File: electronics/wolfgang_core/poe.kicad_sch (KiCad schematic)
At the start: 0 parts

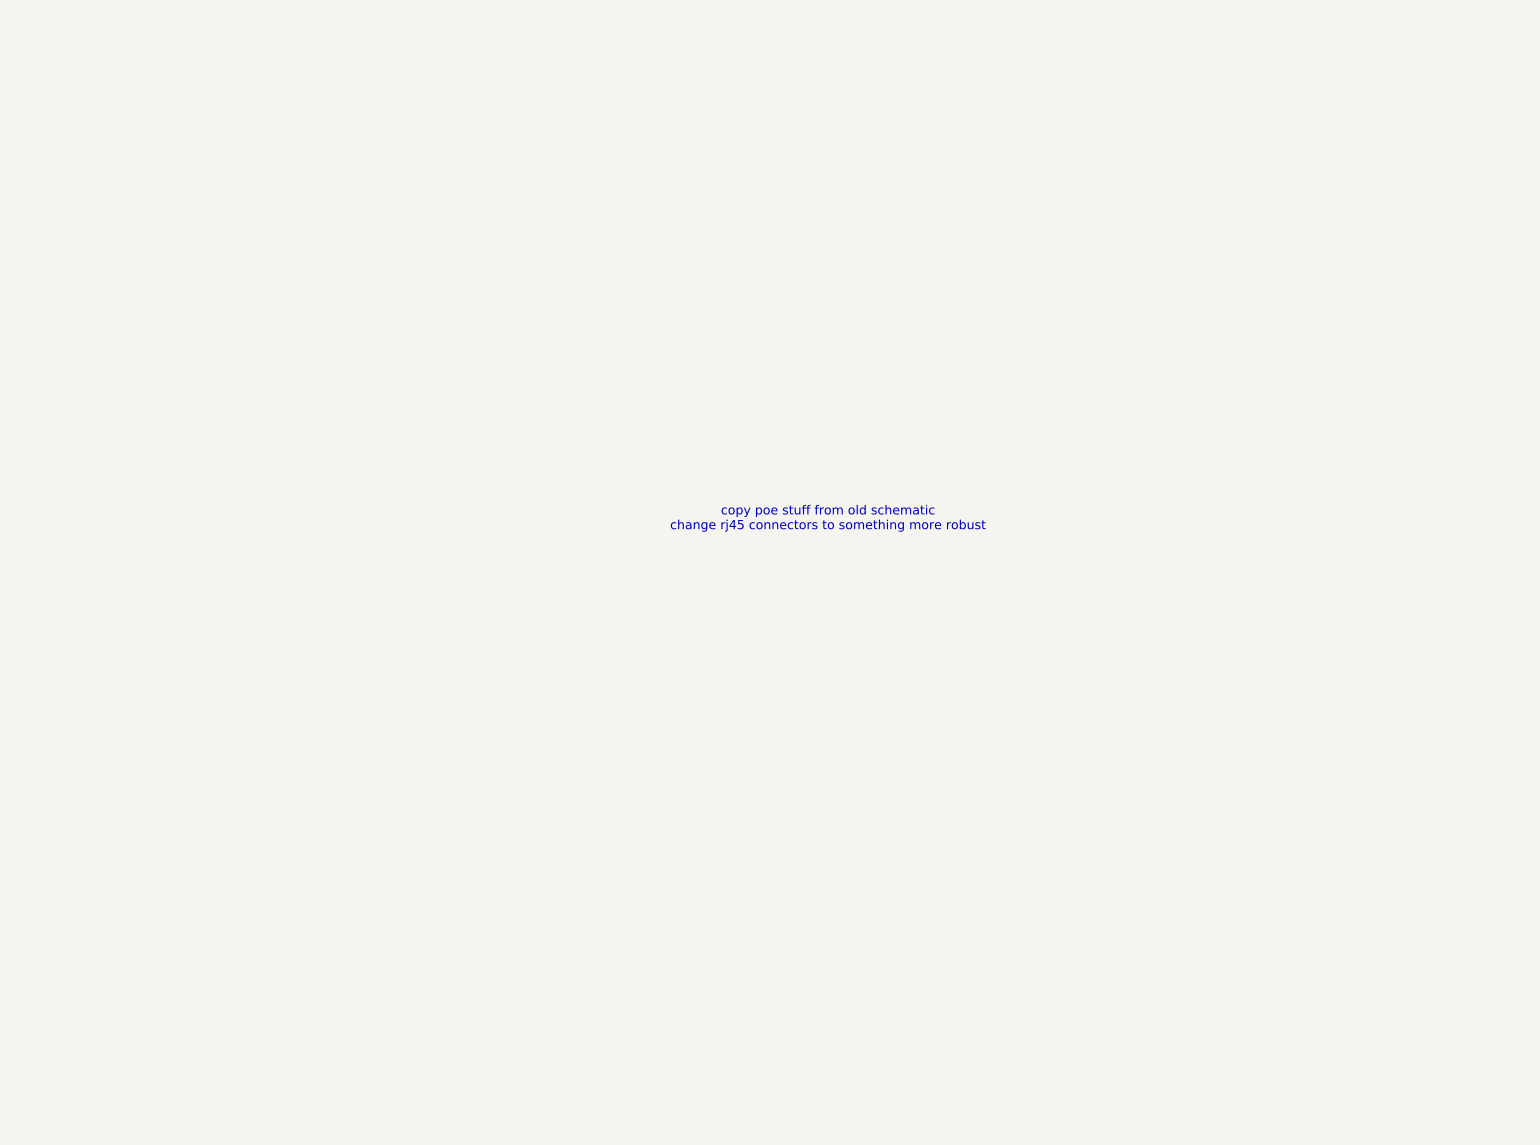
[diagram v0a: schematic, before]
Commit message: Copy over PoE stuff
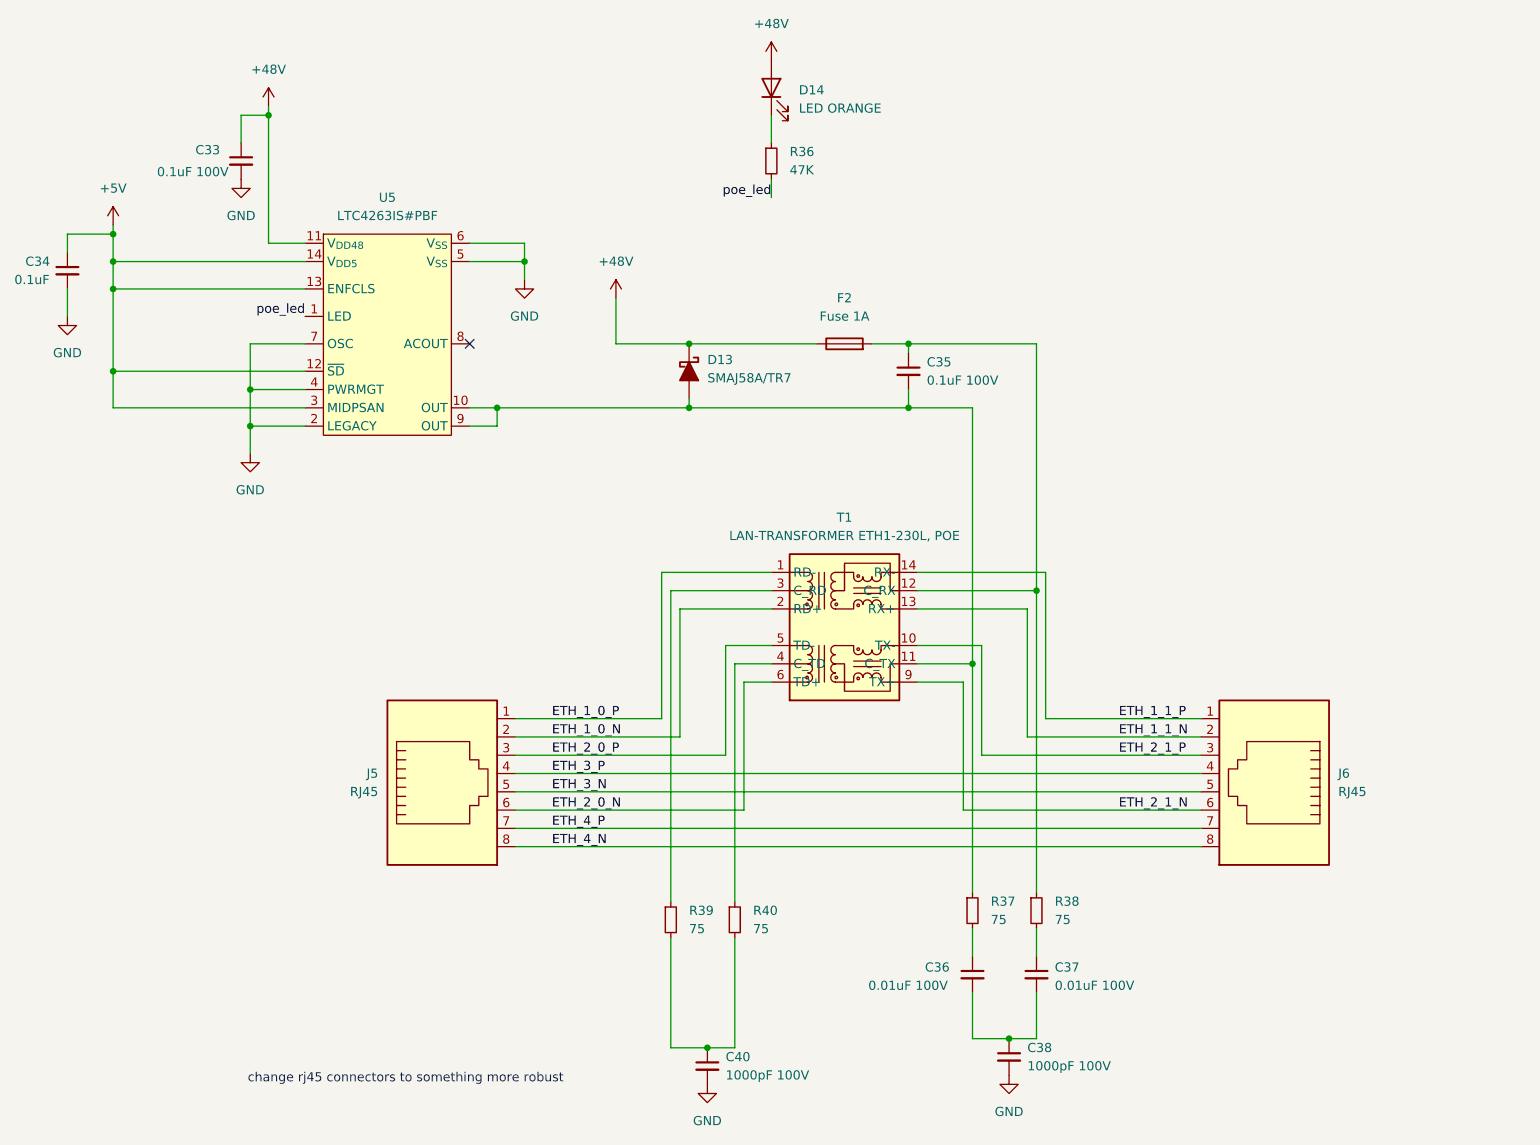
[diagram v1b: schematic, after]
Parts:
- added C33, C35: 0.1uF 100V, symbol Device:C_Small
- added C34: 0.1uF, symbol Device:C_Small
- added C36, C37: 0.01uF 100V, symbol Device:C_Small
- added C38, C40: 1000pF 100V, symbol Device:C_Small
- added D13: SMAJ58A/TR7, symbol Device:D_Schottky_Filled
- added D14: LED ORANGE, symbol Device:LED
- added F2: Fuse 1A, symbol Device:Fuse
- added J5, J6: RJ45, symbol Connector:RJ45
- added R36: 47K, symbol Device:R_Small
- added R37, R38, R39, R40: 75, symbol Device:R_Small
- added T1: LAN-TRANSFORMER ETH1-230L, POE, symbol ETH1-230LD-POE:ETH1-230LD-POE
- added U5: LTC4263IS#PBF, symbol ltc4263:ltc4263
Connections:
- new net: D14.1 (K), R36.1
- new net: C36.2, C37.2, C38.1
- new net: R40.1, T1.4 (C_TD)
- new net: C40.1, R39.2, R40.2
- new net: C35.2, D13.2 (A), R37.1, T1.11 (C_TX), U5.10 (OUT), U5.9 (OUT)
- new net: C36.1, R37.2
- new net: C35.1, F2.2, R38.1, T1.12 (C_RX)
- new net: C37.1, R38.2
- new net: R39.1, T1.3 (C_RD)
- new net +48V: C33.1, D13.1 (K), D14.2 (A), F2.1, U5.11 (V_{DD48})
- new net +5V: C34.1, U5.12 (~{SD}), U5.13 (ENFCLS), U5.14 (V_{DD5}), U5.3 (MIDPSAN)
- new net ETH_1_0_N: J5.2, T1.2 (RD+)
- new net ETH_1_0_P: J5.1, T1.1 (RD-)
- new net ETH_1_1_N: J6.2, T1.13 (RX+)
- new net ETH_1_1_P: J6.1, T1.14 (RX-)
- new net ETH_2_0_N: J5.6, T1.6 (TD+)
- new net ETH_2_0_P: J5.3, T1.5 (TD-)
- new net ETH_2_1_N: J6.6, T1.9 (TX+)
- new net ETH_2_1_P: J6.3, T1.10 (TX-)
- new net ETH_3_N: J5.5, J6.5
- new net ETH_3_P: J5.4, J6.4
- new net ETH_4_N: J5.8, J6.8
- new net ETH_4_P: J5.7, J6.7
- new net GND: C33.2, C34.2, C38.2, C40.2, U5.2 (LEGACY), U5.4 (PWRMGT), U5.5 (V_{SS}), U5.6 (V_{SS}), U5.7 (OSC)
- new net Pad: U5.15 (Pad)
- new net poe_led: R36.2, U5.1 (LED)
- no-connect marks 0 -> 1
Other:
- note added: "change rj45 connectors to something more robust"
- note removed: "copy poe stuff from old schematic change rj45 connectors to something more robust"

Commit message: Footprints hinzugefügt
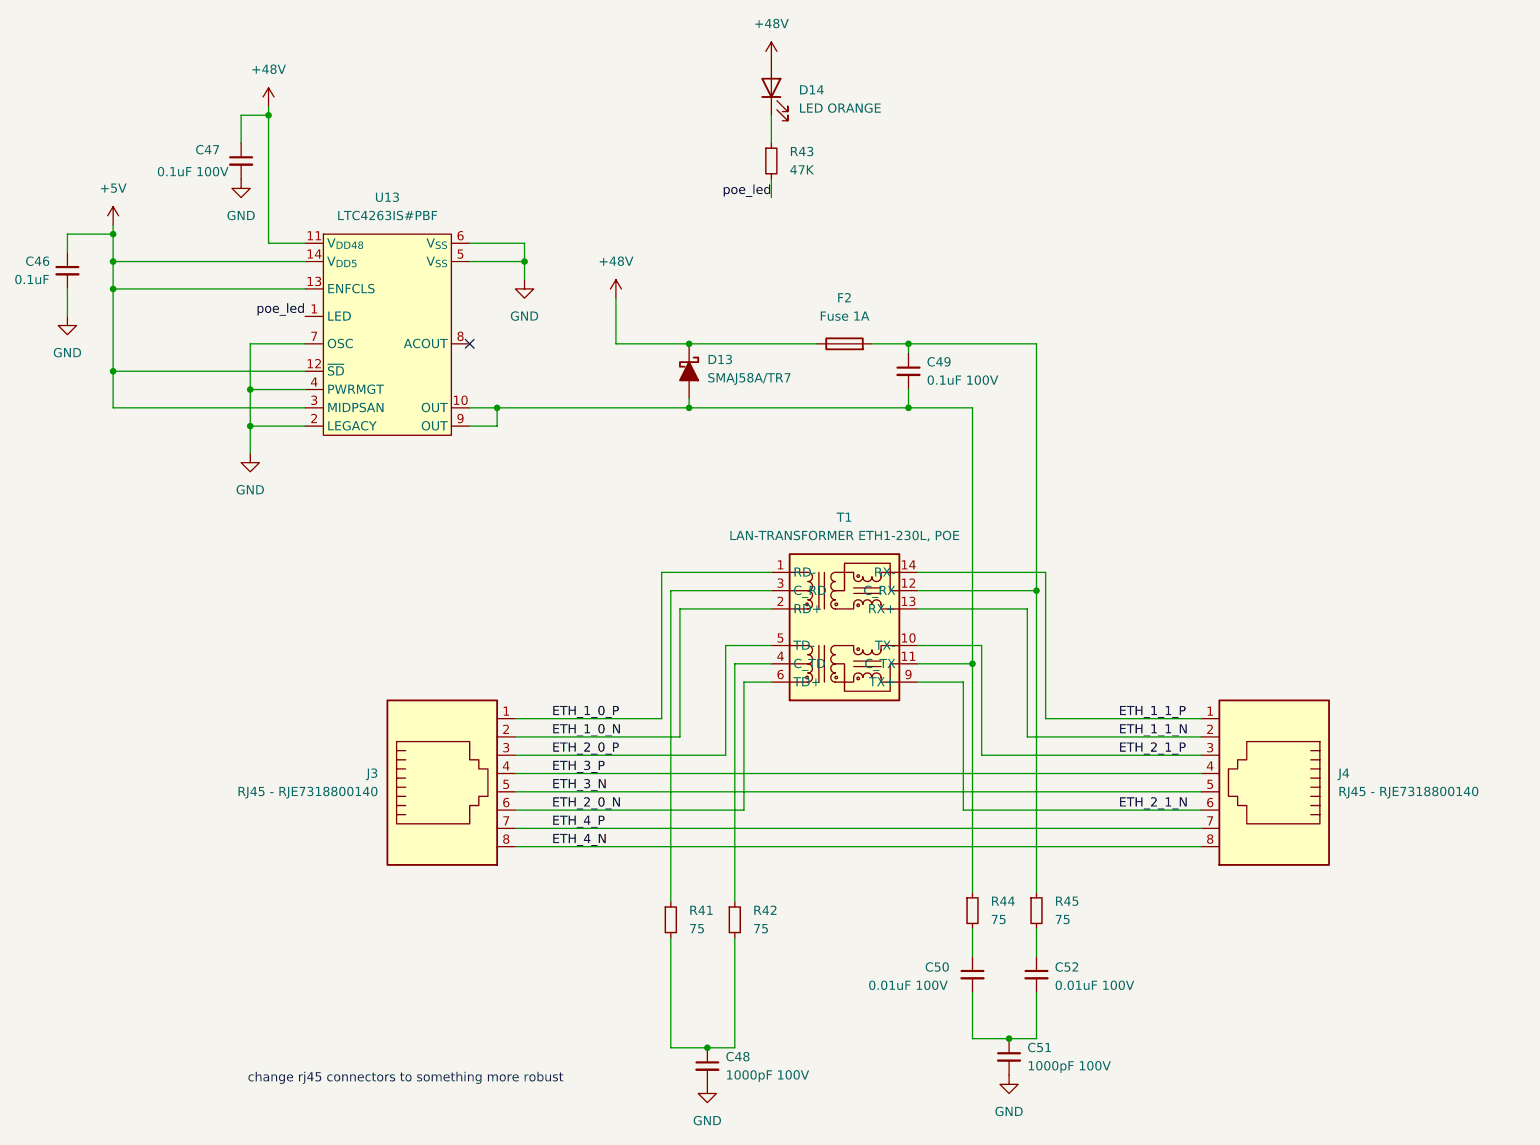
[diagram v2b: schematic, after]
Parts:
- J3: renamed from J5; value RJ45 -> RJ45 - RJE7318800140; footprint (none) -> bitbots:RJE7318800110
- J4: renamed from J6; value RJ45 -> RJ45 - RJE7318800140; footprint (none) -> bitbots:RJE7318800110
- T1: footprint (none) -> bitbots:ETH1230LD
- U13: renamed from U5; footprint (none) -> bitbots:SOIC127P599X175-14N
- renumbered C34 to C46, C33 to C47, C40 to C48, C35 to C49, C36 to C50, C38 to C51, C37 to C52, R39 to R41, R40 to R42, R36 to R43, R37 to R44, R38 to R45
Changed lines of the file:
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@@
 		(dnp no)
 		(fields_autoplaced yes)
-		(property "Reference" "R36"
+		(property "Reference" "R43"
 			(at 123.19 34.2899 0)
 			(effects
@@
 			(project ""
 				(path "/9538e4ed-27e6-4c37-b989-9859dc0d49e8/3d827942-3ef6-4515-bd08-bedcdbccf816"
-					(reference "R36")
+					(reference "R43")
 					(unit 1)
 				)
@@
 		(dnp no)
 		(fields_autoplaced yes)
-		(property "Reference" "C38"
+		(property "Reference" "C51"
 			(at 156.21 158.7562 0)
 			(effects
@@
 			(project ""
 				(path "/9538e4ed-27e6-4c37-b989-9859dc0d49e8/3d827942-3ef6-4515-bd08-bedcdbccf816"
-					(reference "C38")
+					(reference "C51")
 					(unit 1)
 				)
@@
 		(dnp no)
 		(fields_autoplaced yes)
-		(property "Reference" "R40"
+		(property "Reference" "R42"
 			(at 118.11 139.6999 0)
 			(effects
@@
 			(project "wolfgang_core"
 				(path "/9538e4ed-27e6-4c37-b989-9859dc0d49e8/3d827942-3ef6-4515-bd08-bedcdbccf816"
-					(reference "R40")
+					(reference "R42")
 					(unit 1)
 				)
@@
 		(dnp no)
 		(fields_autoplaced yes)
-		(property "Reference" "#PWR090"
+		(property "Reference" "#PWR0108"
 			(at 111.76 170.18 0)
 			(effects
@@
 			(project "wolfgang_core"
 				(path "/9538e4ed-27e6-4c37-b989-9859dc0d49e8/3d827942-3ef6-4515-bd08-bedcdbccf816"
-					(reference "#PWR090")
+					(reference "#PWR0108")
 					(unit 1)
 				)
@@
 		(dnp no)
 		(fields_autoplaced yes)
-		(property "Reference" "U5"
+		(property "Reference" "U13"
 			(at 67.31 40.64 0)
 			(effects
@@
 			)
 		)
-		(property "Footprint" ""
+		(property "Footprint" "bitbots:SOIC127P599X175-14N"
 			(at 66.04 55.88 0)
 			(effects
@@
 			(project ""
 				(path "/9538e4ed-27e6-4c37-b989-9859dc0d49e8/3d827942-3ef6-4515-bd08-bedcdbccf816"
-					(reference "U5")
+					(reference "U13")
 					(unit 1)
 				)
@@
 		(dnp no)
 		(fields_autoplaced yes)
-		(property "Reference" "R37"
+		(property "Reference" "R44"
 			(at 151.13 138.4299 0)
 			(effects
@@
 			(project ""
 				(path "/9538e4ed-27e6-4c37-b989-9859dc0d49e8/3d827942-3ef6-4515-bd08-bedcdbccf816"
-					(reference "R37")
+					(reference "R44")
 					(unit 1)
 				)
@@
 		(dnp no)
 		(fields_autoplaced yes)
-		(property "Reference" "#PWR083"
+		(property "Reference" "#PWR0102"
 			(at 29.21 48.26 0)
 			(effects
@@
 			(project ""
 				(path "/9538e4ed-27e6-4c37-b989-9859dc0d49e8/3d827942-3ef6-4515-bd08-bedcdbccf816"
-					(reference "#PWR083")
+					(reference "#PWR0102")
 					(unit 1)
 				)
@@
 		(dnp no)
 		(fields_autoplaced yes)
-		(property "Reference" "#PWR085"
+		(property "Reference" "#PWR0106"
 			(at 86.36 58.42 0)
 			(effects
@@
 			(project ""
 				(path "/9538e4ed-27e6-4c37-b989-9859dc0d49e8/3d827942-3ef6-4515-bd08-bedcdbccf816"
-					(reference "#PWR085")
+					(reference "#PWR0106")
 					(unit 1)
 				)
@@
 		(dnp no)
 		(fields_autoplaced yes)
-		(property "Reference" "#PWR086"
+		(property "Reference" "#PWR0107"
 			(at 99.06 58.42 0)
 			(effects
@@
 			(project ""
 				(path "/9538e4ed-27e6-4c37-b989-9859dc0d49e8/3d827942-3ef6-4515-bd08-bedcdbccf816"
-					(reference "#PWR086")
+					(reference "#PWR0107")
 					(unit 1)
 				)
@@
 		(on_board yes)
 		(dnp no)
-		(property "Reference" "C36"
+		(property "Reference" "C50"
 			(at 141.986 147.574 0)
 			(effects
@@
 			(project ""
 				(path "/9538e4ed-27e6-4c37-b989-9859dc0d49e8/3d827942-3ef6-4515-bd08-bedcdbccf816"
-					(reference "C36")
+					(reference "C50")
 					(unit 1)
 				)
@@
 		(dnp no)
 		(fields_autoplaced yes)
-		(property "Reference" "#PWR088"
+		(property "Reference" "#PWR0109"
 			(at 120.65 25.4 0)
 			(effects
@@
 			(project ""
 				(path "/9538e4ed-27e6-4c37-b989-9859dc0d49e8/3d827942-3ef6-4515-bd08-bedcdbccf816"
-					(reference "#PWR088")
+					(reference "#PWR0109")
 					(unit 1)
 				)
@@
 		(dnp no)
 		(fields_autoplaced yes)
-		(property "Reference" "#PWR082"
+		(property "Reference" "#PWR0103"
 			(at 46.99 44.45 0)
 			(effects
@@
 			(project ""
 				(path "/9538e4ed-27e6-4c37-b989-9859dc0d49e8/3d827942-3ef6-4515-bd08-bedcdbccf816"
-					(reference "#PWR082")
+					(reference "#PWR0103")
 					(unit 1)
 				)
@@
 		(on_board yes)
 		(dnp no)
-		(property "Reference" "J6"
+		(property "Reference" "J4"
 			(at 199.39 120.6499 0)
 			(effects
@@
 			)
 		)
-		(property "Value" "RJ45"
+		(property "Value" "RJ45 - RJE7318800140"
 			(at 199.39 123.1899 0)
 			(effects
@@
 			)
 		)
-		(property "Footprint" ""
+		(property "Footprint" "bitbots:RJE7318800110"
 			(at 190.5 121.285 90)
 			(effects
@@
 			(project "wolfgang_core"
 				(path "/9538e4ed-27e6-4c37-b989-9859dc0d49e8/3d827942-3ef6-4515-bd08-bedcdbccf816"
-					(reference "J6")
+					(reference "J4")
 					(unit 1)
 				)
@@
 		(dnp no)
 		(fields_autoplaced yes)
-		(property "Reference" "C40"
+		(property "Reference" "C48"
 			(at 114.3 160.0262 0)
 			(effects
@@
 			(project "wolfgang_core"
 				(path "/9538e4ed-27e6-4c37-b989-9859dc0d49e8/3d827942-3ef6-4515-bd08-bedcdbccf816"
-					(reference "C40")
+					(reference "C48")
 					(unit 1)
 				)
@@
 		(dnp no)
 		(fields_autoplaced yes)
-		(property "Reference" "#PWR089"
+		(property "Reference" "#PWR0110"
 			(at 153.67 168.91 0)
 			(effects
@@
 			(project ""
 				(path "/9538e4ed-27e6-4c37-b989-9859dc0d49e8/3d827942-3ef6-4515-bd08-bedcdbccf816"
-					(reference "#PWR089")
+					(reference "#PWR0110")
 					(unit 1)
 				)
@@
 		(dnp no)
 		(fields_autoplaced yes)
-		(property "Reference" "#PWR081"
+		(property "Reference" "#PWR0105"
 			(at 50.8 31.75 0)
 			(effects
@@
 			(project ""
 				(path "/9538e4ed-27e6-4c37-b989-9859dc0d49e8/3d827942-3ef6-4515-bd08-bedcdbccf816"
-					(reference "#PWR081")
+					(reference "#PWR0105")
 					(unit 1)
 				)
@@
 		(on_board yes)
 		(dnp no)
-		(property "Reference" "C33"
+		(property "Reference" "C47"
 			(at 40.64 34.036 0)
 			(effects
@@
 			(project ""
 				(path "/9538e4ed-27e6-4c37-b989-9859dc0d49e8/3d827942-3ef6-4515-bd08-bedcdbccf816"
-					(reference "C33")
+					(reference "C47")
 					(unit 1)
 				)
@@
 		(dnp no)
 		(fields_autoplaced yes)
-		(property "Reference" "R38"
+		(property "Reference" "R45"
 			(at 160.02 138.4299 0)
 			(effects
@@
 			(project "wolfgang_core"
 				(path "/9538e4ed-27e6-4c37-b989-9859dc0d49e8/3d827942-3ef6-4515-bd08-bedcdbccf816"
-					(reference "R38")
+					(reference "R45")
 					(unit 1)
 				)
@@
 		(dnp no)
 		(fields_autoplaced yes)
-		(property "Reference" "C35"
+		(property "Reference" "C49"
 			(at 142.24 63.5062 0)
 			(effects
@@
 			(project ""
 				(path "/9538e4ed-27e6-4c37-b989-9859dc0d49e8/3d827942-3ef6-4515-bd08-bedcdbccf816"
-					(reference "C35")
+					(reference "C49")
 					(unit 1)
 				)
@@
 		(dnp no)
 		(fields_autoplaced yes)
-		(property "Reference" "R39"
+		(property "Reference" "R41"
 			(at 109.22 139.6999 0)
 			(effects
@@
 			(project "wolfgang_core"
 				(path "/9538e4ed-27e6-4c37-b989-9859dc0d49e8/3d827942-3ef6-4515-bd08-bedcdbccf816"
-					(reference "R39")
+					(reference "R41")
 					(unit 1)
 				)
@@
 		(on_board yes)
 		(dnp no)
-		(property "Reference" "C34"
+		(property "Reference" "C46"
 			(at 17.018 49.53 0)
 			(effects
@@
 			(project ""
 				(path "/9538e4ed-27e6-4c37-b989-9859dc0d49e8/3d827942-3ef6-4515-bd08-bedcdbccf816"
-					(reference "C34")
+					(reference "C46")
 					(unit 1)
 				)
@@
 		(dnp no)
 		(fields_autoplaced yes)
-		(property "Reference" "J5"
+		(property "Reference" "J3"
 			(at 66.04 120.6499 0)
 			(effects
@@
 			)
 		)
-		(property "Value" "RJ45"
+		(property "Value" "RJ45 - RJE7318800140"
 			(at 66.04 123.1899 0)
 			(effects
@@
 			)
 		)
-		(property "Footprint" ""
+		(property "Footprint" "bitbots:RJE7318800110"
 			(at 74.93 121.285 90)
 			(effects
@@
 			(project ""
 				(path "/9538e4ed-27e6-4c37-b989-9859dc0d49e8/3d827942-3ef6-4515-bd08-bedcdbccf816"
-					(reference "J5")
+					(reference "J3")
 					(unit 1)
 				)
@@
 		(dnp no)
 		(fields_autoplaced yes)
-		(property "Reference" "#PWR087"
+		(property "Reference" "#PWR0104"
 			(at 48.26 82.55 0)
 			(effects
@@
 			(project ""
 				(path "/9538e4ed-27e6-4c37-b989-9859dc0d49e8/3d827942-3ef6-4515-bd08-bedcdbccf816"
-					(reference "#PWR087")
+					(reference "#PWR0104")
 					(unit 1)
 				)
@@
 			)
 		)
-		(property "Footprint" ""
+		(property "Footprint" "bitbots:ETH1230LD"
 			(at 130.81 100.33 0)
 			(effects
@@
 		(on_board yes)
 		(dnp no)
-		(property "Reference" "C37"
+		(property "Reference" "C52"
 			(at 160.02 147.574 0)
 			(effects
@@
 			(project "wolfgang_core"
 				(path "/9538e4ed-27e6-4c37-b989-9859dc0d49e8/3d827942-3ef6-4515-bd08-bedcdbccf816"
-					(reference "C37")
+					(reference "C52")
 					(unit 1)
 				)
@@
 		(dnp no)
 		(fields_autoplaced yes)
-		(property "Reference" "#PWR084"
+		(property "Reference" "#PWR0101"
 			(at 22.86 63.5 0)
 			(effects
@@
 			(project ""
 				(path "/9538e4ed-27e6-4c37-b989-9859dc0d49e8/3d827942-3ef6-4515-bd08-bedcdbccf816"
-					(reference "#PWR084")
-					(unit 1)
-				)
+					(reference "#PWR0101")
+					(unit 1)
+				)
